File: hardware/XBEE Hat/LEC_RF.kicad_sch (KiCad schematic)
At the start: 6 parts, among them J1 Conn_Coaxial_Small, J2 Conn_01x04, U1 XBee_SMT, U2 TLV1117-33

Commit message: Push of most recent schematic and PCB
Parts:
- C1, C2: footprint Capacitor_SMD:C_0805_2012Metric -> Capacitor_SMD:C_0603_1608Metric
- U1: footprint RF_Module:Digi_XBee_SMT -> Custom:XBEE_GND_PAD
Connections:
- net GND: now also U1.38 (GND)
- no-connect marks 0 -> 20
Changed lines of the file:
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@@
 	(paper "A4")
+	(junction
+		(at 223.52 109.22)
+		(diameter 0)
+		(color 0 0 0 0)
+	)
+	(junction
+		(at 219.71 109.22)
+		(diameter 0)
+		(color 0 0 0 0)
+	)
 	(junction
 		(at 220.98 109.22)
@@
 		(color 0 0 0 0)
 	)
+	(no_connect
+		(at 190.5 99.06)
+	)
+	(no_connect
+		(at 190.5 93.98)
+	)
+	(no_connect
+		(at 190.5 88.9)
+	)
+	(no_connect
+		(at 190.5 96.52)
+	)
+	(no_connect
+		(at 220.98 55.88)
+	)
+	(no_connect
+		(at 190.5 68.58)
+	)
+	(no_connect
+		(at 246.38 60.96)
+	)
+	(no_connect
+		(at 246.38 63.5)
+	)
+	(no_connect
+		(at 246.38 71.12)
+	)
+	(no_connect
+		(at 190.5 101.6)
+	)
+	(no_connect
+		(at 246.38 68.58)
+	)
+	(no_connect
+		(at 190.5 66.04)
+	)
+	(no_connect
+		(at 190.5 81.28)
+	)
+	(no_connect
+		(at 190.5 73.66)
+	)
+	(no_connect
+		(at 246.38 73.66)
+	)
+	(no_connect
+		(at 246.38 66.04)
+	)
+	(no_connect
+		(at 190.5 76.2)
+	)
+	(no_connect
+		(at 190.5 86.36)
+	)
+	(no_connect
+		(at 190.5 78.74)
+	)
+	(no_connect
+		(at 190.5 104.14)
+	)
 	(wire
 		(pts
@@
 	(wire
 		(pts
-			(xy 218.44 109.22) (xy 218.44 113.03)
-		)
-		(stroke
-			(width 0)
-			(type default)
-		)
-	)
-	(wire
-		(pts
 			(xy 156.21 33.02) (xy 166.37 33.02)
 		)
@@
 	(wire
 		(pts
-			(xy 218.44 109.22) (xy 220.98 109.22)
+			(xy 218.44 109.22) (xy 219.71 109.22)
 		)
 		(stroke
@@
 	(wire
 		(pts
+			(xy 223.52 109.22) (xy 226.06 109.22)
+		)
+		(stroke
+			(width 0)
+			(type default)
+		)
+	)
+	(wire
+		(pts
 			(xy 144.78 33.02) (xy 156.21 33.02)
 		)
@@
 	(wire
 		(pts
+			(xy 219.71 109.22) (xy 220.98 109.22)
+		)
+		(stroke
+			(width 0)
+			(type default)
+		)
+	)
+	(wire
+		(pts
 			(xy 220.98 109.22) (xy 223.52 109.22)
 		)
@@
 		(pts
 			(xy 184.15 60.96) (xy 190.5 60.96)
+		)
+		(stroke
+			(width 0)
+			(type default)
+		)
+	)
+	(wire
+		(pts
+			(xy 219.71 109.22) (xy 219.71 114.3)
 		)
 		(stroke
@@
 	(symbol
 		(lib_id "power:GND")
-		(at 218.44 113.03 0)
+		(at 219.71 114.3 0)
 		(unit 1)
 		(exclude_from_sim no)
@@
 		(fields_autoplaced yes)
 		(property "Reference" "#PWR01"
-			(at 218.44 119.38 0)
+			(at 219.71 120.65 0)
 			(effects
 				(font
@@
 		)
 		(property "Value" "GND"
-			(at 218.44 118.11 0)
+			(at 219.71 119.38 0)
 			(effects
 				(font
@@
 		)
 		(property "Footprint" ""
-			(at 218.44 113.03 0)
+			(at 219.71 114.3 0)
 			(effects
 				(font
@@
 		)
 		(property "Datasheet" ""
-			(at 218.44 113.03 0)
+			(at 219.71 114.3 0)
 			(effects
 				(font
@@
 		)
 		(property "Description" "Power symbol creates a global label with name \"GND\" , ground"
-			(at 218.44 113.03 0)
+			(at 219.71 114.3 0)
 			(effects
 				(font
@@
 			)
 		)
-		(property "Footprint" "Capacitor_SMD:C_0805_2012Metric"
+		(property "Footprint" "Capacitor_SMD:C_0603_1608Metric"
 			(at 156.21 38.1 0)
 			(effects
@@
 			)
 		)
-		(property "Footprint" "RF_Module:Digi_XBee_SMT"
+		(property "Footprint" "Custom:XBEE_GND_PAD"
 			(at 239.776 108.204 0)
 			(effects
@@
 		)
 		(pin "36"
+		)
+		(pin "38"
 		)
 		(instances
@@
 			)
 		)
-		(property "Footprint" "Capacitor_SMD:C_0805_2012Metric"
+		(property "Footprint" "Capacitor_SMD:C_0603_1608Metric"
 			(at 144.78 38.1 0)
 			(effects

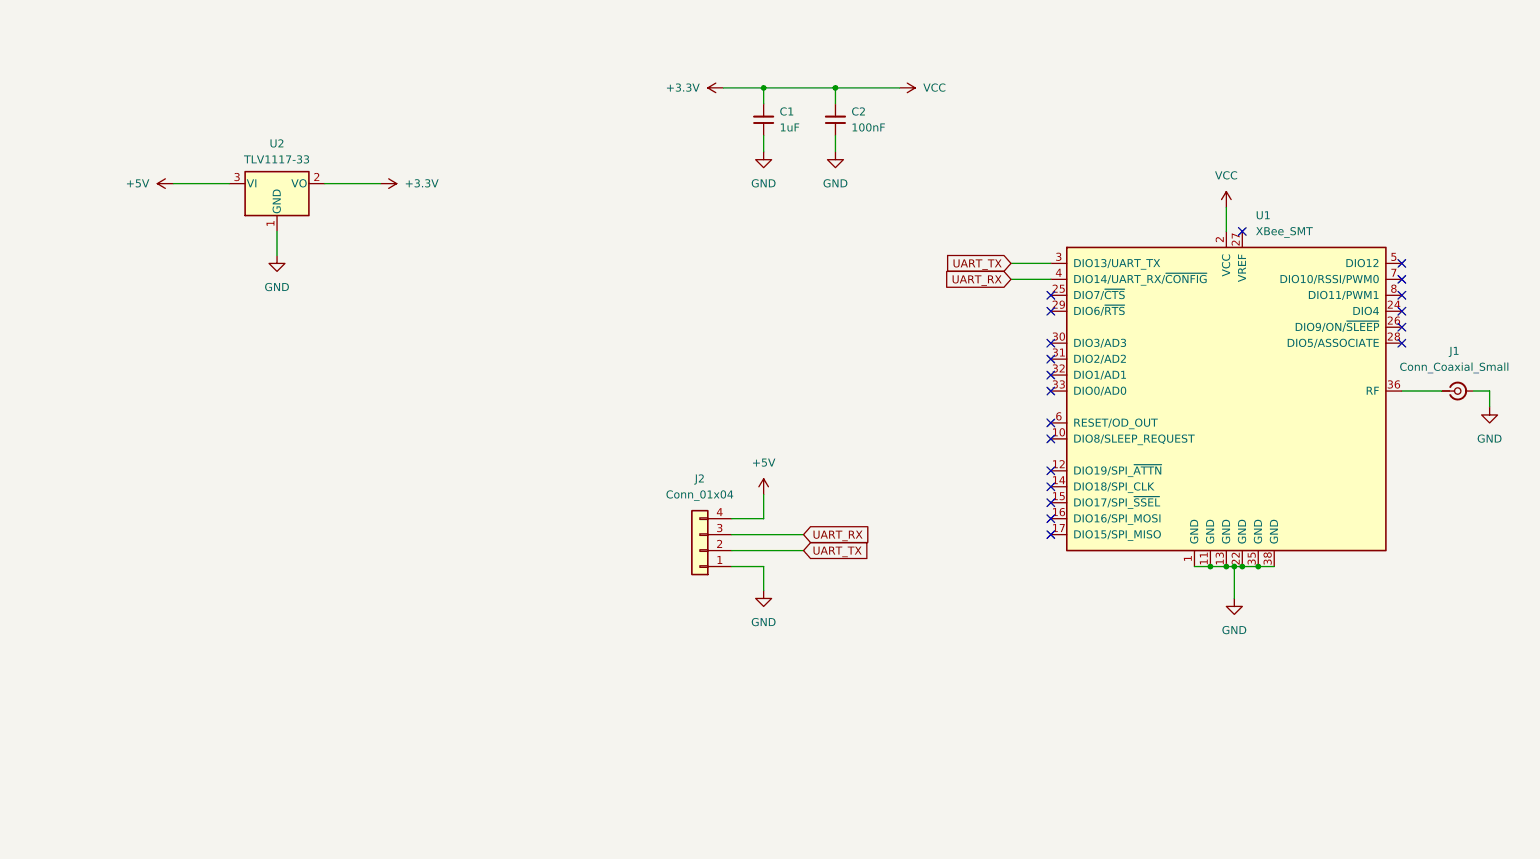
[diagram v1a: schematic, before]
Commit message: Routed XBEE PCB
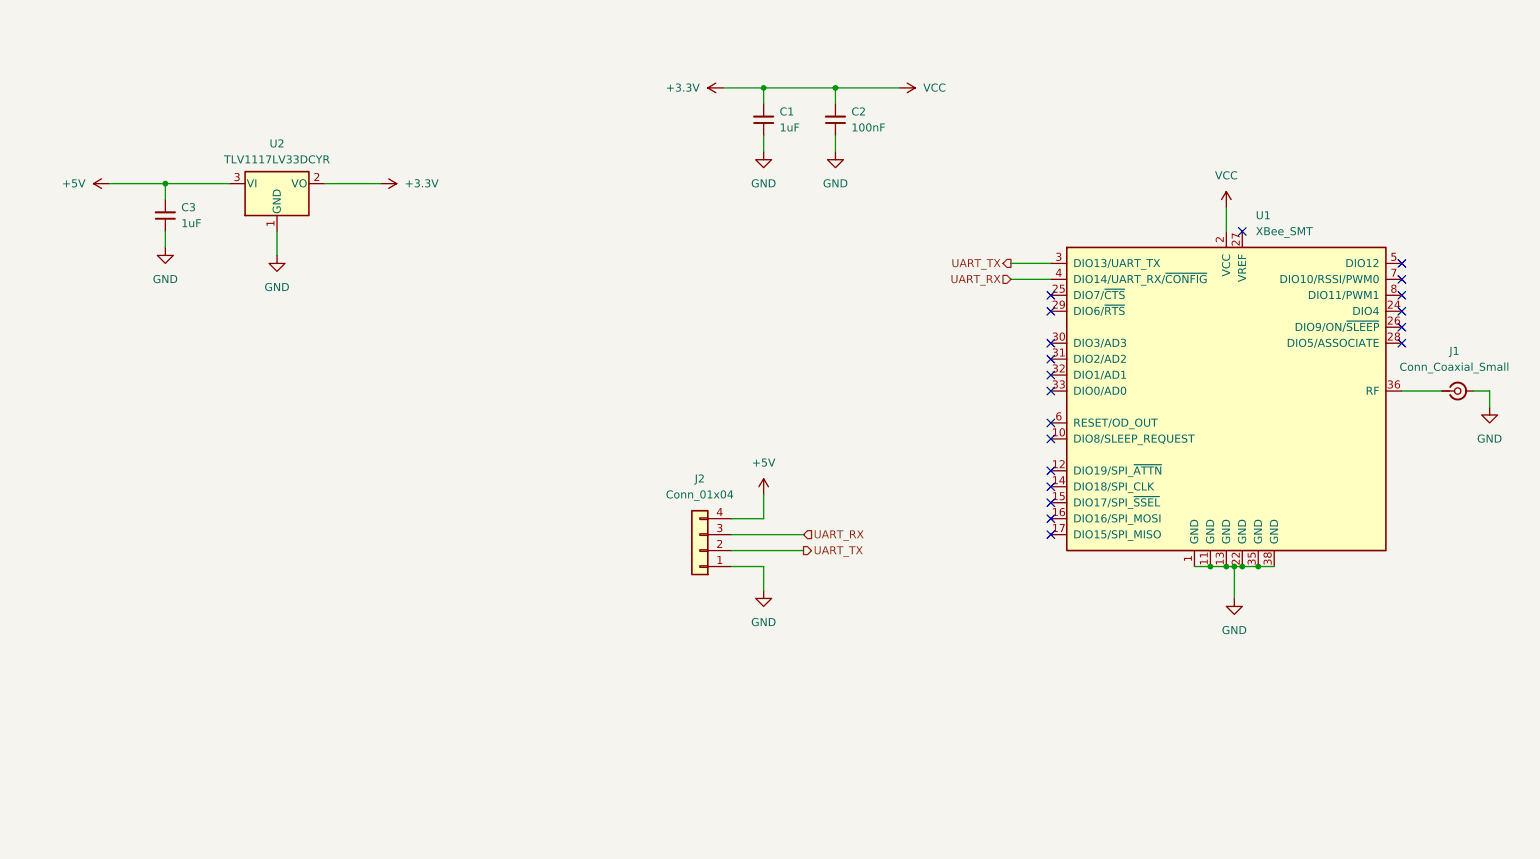
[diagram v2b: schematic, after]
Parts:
- added C3: 1uF, Capacitor_SMD:C_0805_2012Metric, symbol Device:C_Small
- C1: footprint Capacitor_SMD:C_0603_1608Metric -> Capacitor_SMD:C_0805_2012Metric
- U2: value TLV1117-33 -> TLV1117LV33DCYR
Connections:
- net +5V: now also C3.2
- net GND: now also C3.1
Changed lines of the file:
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@@
+	)
+	(junction
+		(at 49.53 48.26)
+		(diameter 0)
+		(color 0 0 0 0)
 	)
 	(junction
@@
 	(wire
 		(pts
+			(xy 49.53 55.88) (xy 49.53 58.42)
+		)
+		(stroke
+			(width 0)
+			(type default)
+		)
+	)
+	(wire
+		(pts
 			(xy 156.21 33.02) (xy 166.37 33.02)
 		)
@@
 	(wire
 		(pts
+			(xy 49.53 48.26) (xy 59.69 48.26)
+		)
+		(stroke
+			(width 0)
+			(type default)
+		)
+	)
+	(wire
+		(pts
 			(xy 139.7 109.22) (xy 144.78 109.22)
 		)
@@
 	(wire
 		(pts
-			(xy 50.8 48.26) (xy 59.69 48.26)
+			(xy 40.64 48.26) (xy 49.53 48.26)
 		)
 		(stroke
@@
 	(wire
 		(pts
+			(xy 49.53 48.26) (xy 49.53 50.8)
+		)
+		(stroke
+			(width 0)
+			(type default)
+		)
+	)
+	(wire
+		(pts
 			(xy 246.38 81.28) (xy 252.73 81.28)
 		)
@@
 		)
 	)
-	(global_label "UART_TX"
-		(shape input)
-		(at 151.13 106.68 0)
-		(fields_autoplaced yes)
+	(hierarchical_label "UART_TX"
+		(shape output)
+		(at 184.15 60.96 180)
 		(effects
 			(font
 				(size 1.27 1.27)
 			)
-			(justify left)
-		)
-		(property "Intersheetrefs" "${INTERSHEET_REFS}"
-			(at 161.9166 106.68 0)
-			(effects
-				(font
-					(size 1.27 1.27)
-				)
-				(justify left)
-				(hide yes)
-			)
-		)
-	)
-	(global_label "UART_RX"
+			(justify right)
+		)
+	)
+	(hierarchical_label "UART_RX"
 		(shape input)
 		(at 151.13 104.14 0)
-		(fields_autoplaced yes)
 		(effects
 			(font
@@
 			(justify left)
 		)
-		(property "Intersheetrefs" "${INTERSHEET_REFS}"
-			(at 162.219 104.14 0)
-			(effects
-				(font
-					(size 1.27 1.27)
-				)
-				(justify left)
-				(hide yes)
-			)
-		)
-	)
-	(global_label "UART_TX"
-		(shape input)
-		(at 184.15 60.96 180)
-		(fields_autoplaced yes)
+	)
+	(hierarchical_label "UART_TX"
+		(shape output)
+		(at 151.13 106.68 0)
 		(effects
 			(font
 				(size 1.27 1.27)
 			)
-			(justify right)
-		)
-		(property "Intersheetrefs" "${INTERSHEET_REFS}"
-			(at 173.3634 60.96 0)
-			(effects
-				(font
-					(size 1.27 1.27)
-				)
-				(justify right)
-				(hide yes)
-			)
-		)
-	)
-	(global_label "UART_RX"
+			(justify left)
+		)
+	)
+	(hierarchical_label "UART_RX"
 		(shape input)
 		(at 184.15 63.5 180)
-		(fields_autoplaced yes)
 		(effects
 			(font
@@
 			)
 			(justify right)
-		)
-		(property "Intersheetrefs" "${INTERSHEET_REFS}"
-			(at 173.061 63.5 0)
-			(effects
-				(font
-					(size 1.27 1.27)
-				)
-				(justify right)
-				(hide yes)
-			)
 		)
 	)
@@
 	(symbol
 		(lib_id "power:+5V")
-		(at 50.8 48.26 90)
+		(at 40.64 48.26 90)
 		(unit 1)
 		(exclude_from_sim no)
@@
 		(fields_autoplaced yes)
 		(property "Reference" "#PWR010"
-			(at 54.61 48.26 0)
+			(at 44.45 48.26 0)
 			(effects
 				(font
@@
 		)
 		(property "Value" "+5V"
-			(at 46.99 48.2599 90)
+			(at 36.83 48.2599 90)
 			(effects
 				(font
@@
 		)
 		(property "Footprint" ""
-			(at 50.8 48.26 0)
+			(at 40.64 48.26 0)
 			(effects
 				(font
@@
 		)
 		(property "Datasheet" ""
-			(at 50.8 48.26 0)
+			(at 40.64 48.26 0)
 			(effects
 				(font
@@
 		)
 		(property "Description" "Power symbol creates a global label with name \"+5V\""
-			(at 50.8 48.26 0)
+			(at 40.64 48.26 0)
 			(effects
 				(font
@@
 	(symbol
 		(lib_id "power:GND")
+		(at 49.53 58.42 0)
+		(unit 1)
+		(exclude_from_sim no)
+		(in_bom yes)
+		(on_board yes)
+		(dnp no)
+		(fields_autoplaced yes)
+		(property "Reference" "#PWR012"
+			(at 49.53 64.77 0)
+			(effects
+				(font
+					(size 1.27 1.27)
+				)
+				(hide yes)
+			)
+		)
+		(property "Value" "GND"
+			(at 49.53 63.5 0)
+			(effects
+				(font
+					(size 1.27 1.27)
+				)
+			)
+		)
+		(property "Footprint" ""
+			(at 49.53 58.42 0)
+			(effects
+				(font
+					(size 1.27 1.27)
+				)
+				(hide yes)
+			)
+		)
+		(property "Datasheet" ""
+			(at 49.53 58.42 0)
+			(effects
+				(font
+					(size 1.27 1.27)
+				)
+				(hide yes)
+			)
+		)
+		(property "Description" "Power symbol creates a global label with name \"GND\" , ground"
+			(at 49.53 58.42 0)
+			(effects
+				(font
+					(size 1.27 1.27)
+				)
+				(hide yes)
+			)
+		)
+		(pin "1"
+		)
+		(instances
+			(project ""
+				(path "/e1c8f876-6e96-4127-b3a1-831dc1ec7ba6"
+					(reference "#PWR012")
+					(unit 1)
+				)
+			)
+		)
+	)
+	(symbol
+		(lib_id "power:GND")
 		(at 144.78 43.18 0)
 		(unit 1)
@@
 	(symbol
 		(lib_id "Device:C_Small")
+		(at 49.53 53.34 180)
+		(unit 1)
+		(exclude_from_sim no)
+		(in_bom yes)
+		(on_board yes)
+		(dnp no)
+		(fields_autoplaced yes)
+		(property "Reference" "C3"
+			(at 52.07 52.0635 0)
+			(effects
+				(font
+					(size 1.27 1.27)
+				)
+				(justify right)
+			)
+		)
+		(property "Value" "1uF"
+			(at 52.07 54.6035 0)
+			(effects
+				(font
+					(size 1.27 1.27)
+				)
+				(justify right)
+			)
+		)
+		(property "Footprint" "Capacitor_SMD:C_0805_2012Metric"
+			(at 49.53 53.34 0)
+			(effects
+				(font
+					(size 1.27 1.27)
+				)
+				(hide yes)
+			)
+		)
+		(property "Datasheet" "~"
+			(at 49.53 53.34 0)
+			(effects
+				(font
+					(size 1.27 1.27)
+				)
+				(hide yes)
+			)
+		)
+		(property "Description" "Unpolarized capacitor, small symbol"
+			(at 49.53 53.34 0)
+			(effects
+				(font
+					(size 1.27 1.27)
+				)
+				(hide yes)
+			)
+		)
+		(pin "2"
+		)
+		(pin "1"
+		)
+		(instances
+			(project ""
+				(path "/e1c8f876-6e96-4127-b3a1-831dc1ec7ba6"
+					(reference "C3")
+					(unit 1)
+				)
+			)
+		)
+	)
+	(symbol
+		(lib_id "Device:C_Small")
 		(at 156.21 38.1 180)
 		(unit 1)
@@
 			)
 		)
-		(property "Value" "TLV1117-33"
+		(property "Value" "TLV1117LV33DCYR"
 			(at 67.31 44.45 0)
 			(effects
@@
 			)
 		)
-		(property "Description" "800mA Low-Dropout Linear Regulator, 3.3V fixed output, TO-220/TO-252/TO-263/SOT-223"
+		(property "Description" "1A Low-Dropout Linear Regulator, 3.3V fixed output, TO-220/TO-252/TO-263/SOT-223"
 			(at 67.31 48.26 0)
 			(effects
@@
 			)
 		)
-		(property "Footprint" "Capacitor_SMD:C_0603_1608Metric"
+		(property "Footprint" "Capacitor_SMD:C_0805_2012Metric"
 			(at 144.78 38.1 0)
 			(effects

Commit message: Final revision of XBEE board
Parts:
- removed J1: Conn_Coaxial_Small, Connector_Coaxial:SMA_Wurth_60312002114503_Vertical, symbol Connector:Conn_Coaxial_Small
- added C4: 1nF, Capacitor_SMD:C_0805_2012Metric, symbol Device:C_Small
- added R1: 300, Resistor_SMD:R_0805_2012Metric, symbol Device:R
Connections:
- net +3.3V: now also R1.1; no longer C1.2, C2.2, U1.2 (VCC)
- net GND: now also C4.1
- new net VCC: C1.2, C2.2, C4.2, R1.2, U1.2 (VCC)
- no-connect marks 20 -> 21

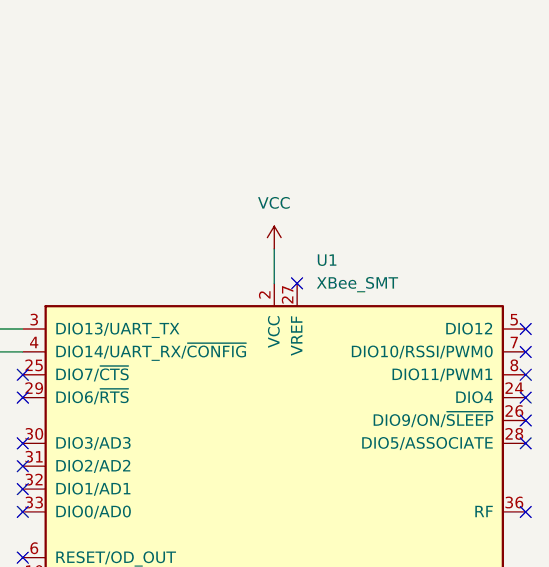
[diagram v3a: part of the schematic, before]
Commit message: Added part numbers and datasheets
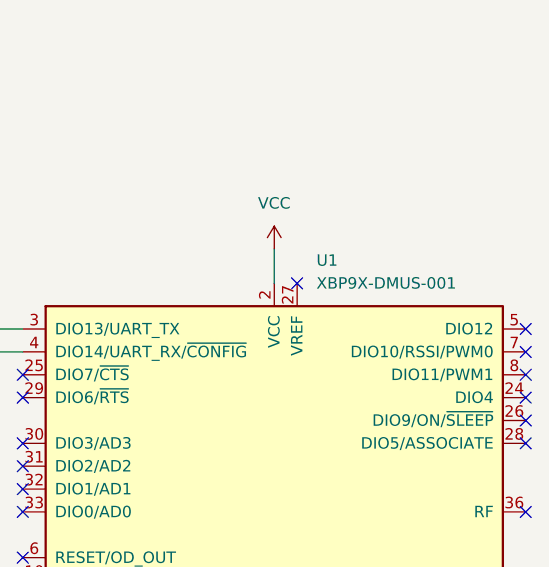
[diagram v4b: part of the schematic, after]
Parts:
- U1: value XBee_SMT -> XBP9X-DMUS-001
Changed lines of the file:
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@@
 			)
 		)
-		(property "Datasheet" "~"
+		(property "Datasheet" "https://www.digikey.com/en/products/detail/kemet/C0805C102F5HACAUTO/7958273"
 			(at 135.89 38.1 0)
 			(effects
@@
 			)
 		)
-		(property "Datasheet" "~"
+		(property "Datasheet" "https://www.digikey.com/en/products/detail/samsung-electro-mechanics/CL21Y105KCYVPNE/14565404"
 			(at 49.53 53.34 0)
 			(effects
@@
 			)
 		)
-		(property "Datasheet" "~"
+		(property "Datasheet" "https://www.digikey.com/en/products/detail/samsung-electro-mechanics/CL10B104KB8NNNC/3886658"
 			(at 156.21 38.1 0)
 			(effects
@@
 			)
 		)
-		(property "Datasheet" "~"
+		(property "Datasheet" "https://www.digikey.com/en/products/detail/panasonic-electronic-components/ERA-6AEB301V/1465735"
 			(at 130.81 33.02 0)
 			(effects
@@
 			)
 		)
-		(property "Value" "XBee_SMT"
+		(property "Value" "XBP9X-DMUS-001"
 			(at 223.1233 55.88 0)
 			(effects
@@
 			)
 		)
-		(property "Datasheet" "http://www.digi.com/resources/documentation/digidocs/pdfs/90002126.pdf"
+		(property "Datasheet" "https://www.digikey.com/en/products/detail/digi/XBP9X-DMUS-001/5972744"
 			(at 218.44 91.44 0)
 			(effects
@@
 			)
 		)
-		(property "Datasheet" "~"
+		(property "Datasheet" "https://www.digikey.com/en/products/detail/samsung-electro-mechanics/CL21Y105KCYVPNE/14565404"
 			(at 144.78 38.1 0)
 			(effects

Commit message: Done
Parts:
- removed C1, C3: 1uF, Capacitor_SMD:C_0805_2012Metric, symbol Device:C_Small
- removed C2: 100nF, Capacitor_SMD:C_0603_1608Metric, symbol Device:C_Small
- removed C4: 1nF, Capacitor_SMD:C_0805_2012Metric, symbol Device:C_Small
- removed R1: 300, Resistor_SMD:R_0805_2012Metric, symbol Device:R
- removed U2: TLV1117LV33DCYR, Package_TO_SOT_SMD:SOT-223-3_TabPin2, symbol Regulator_Linear:TLV1117-33
- added C1: 22uF, Capacitor_SMD:C_0805_2012Metric, symbol Device:C_Polarized_Small
- added C10: 1u, Capacitor_SMD:C_0805_2012Metric, symbol Device:C
- added C2: 10u, Capacitor_SMD:C_1210_3225Metric, symbol Device:C
- added C3: 10uF, Capacitor_SMD:C_0805_2012Metric, symbol Device:C_Polarized_Small
- added C4, C5, C6: 100n, Capacitor_SMD:C_0603_1608Metric, symbol Device:C
- added CR1: LD1086DT33TR, Package_TO_SOT_SMD:TO-252-2, symbol LD1086DT33TR:LD1086DT33TR
- added FB1: FerriteBead, Resistor_SMD:R_0603_1608Metric, symbol Device:FerriteBead
- U1: DigiKey (none) -> https://www.digikey.com/en/products/detail/digi/XBP9X-DMUS-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
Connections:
- net +5V: now also C5.2, FB1.1
- net GND: now also C1.2, C10.2, C2.2, C3.2, C4.1, C5.1, C6.1, CR1.1 (ADJ/GND)
- net VCC: now also C1.1, C10.1, C2.1, C4.2, CR1.2 (OUTPUT)
- new net +5V_Filt: C3.1, C6.2, CR1.3 (INPUT), FB1.2
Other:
- moved on the sheet: J2, U1
